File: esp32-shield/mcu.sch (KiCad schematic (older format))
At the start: 31 parts, among them J11 DNP, J5 Conn_01x14_Female, J6 Conn_01x14_Female, Q3 S8050, Q4 S8050, SW1 SKRKAEE020, U13 ESP32-WROOM32, U14 W25Q32JVSS, U4 SN74LV1T34DBV, U5 CH340C, U6 AMS1117-3.3, Y1 12MHZ

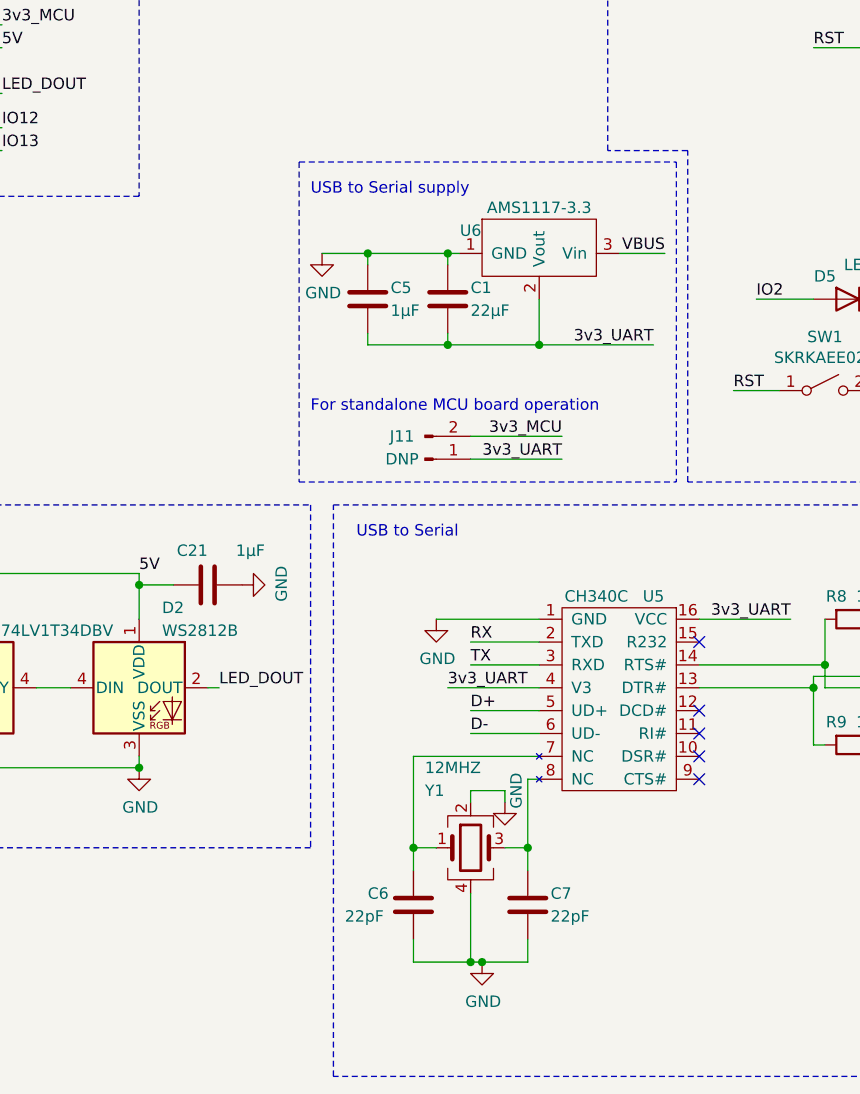
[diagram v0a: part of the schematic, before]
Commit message: changed CH340G to CH340C, deleted crystal footprint and caps, added caps
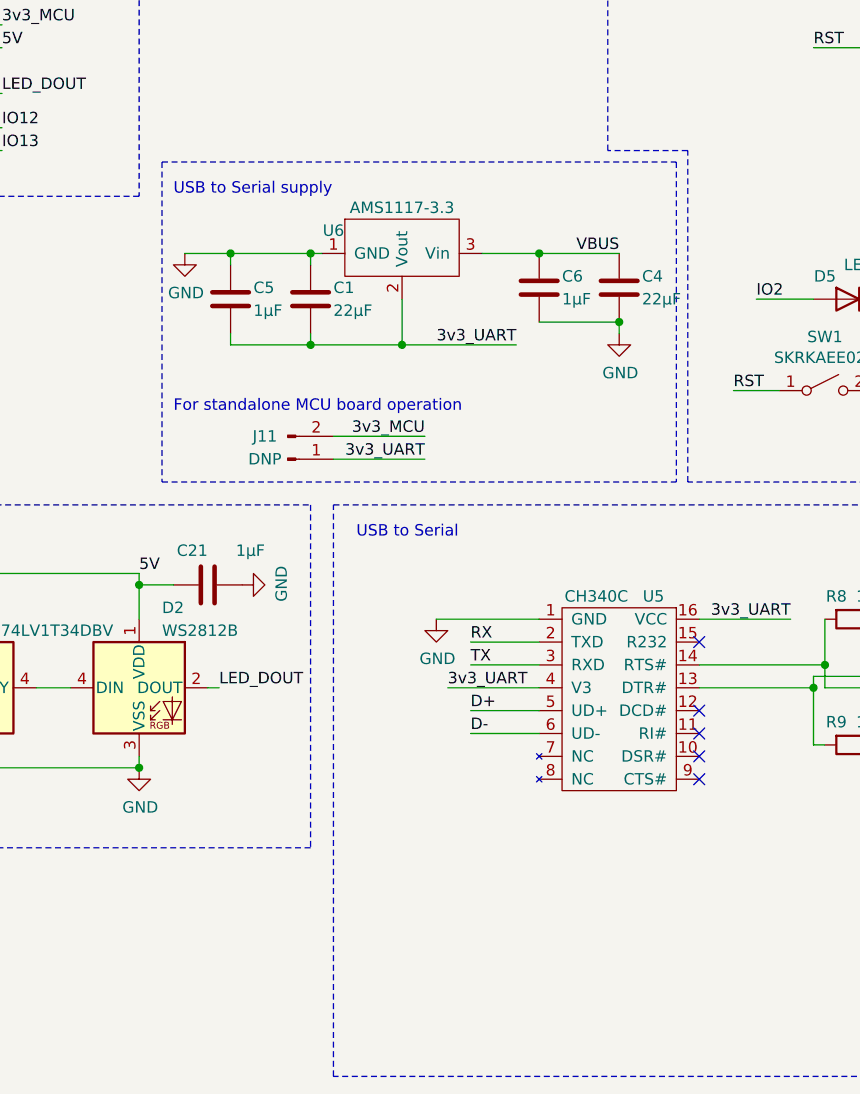
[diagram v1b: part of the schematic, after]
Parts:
- removed C7: 22pF, Capacitor_SMD:C_0603_1608Metric_Pad1.05x0.95mm_HandSolder, symbol Device:C
- removed Y1: 12MHZ, Crystal:Crystal_SMD_3225-4Pin_3.2x2.5mm_HandSoldering, symbol Device:Crystal_GND24
- added C4: 22µF, Capacitor_SMD:C_0805_2012Metric, symbol Device:C
- C19, C20, C21, C26, C5: footprint Capacitor_SMD:C_0603_1608Metric_Pad1.05x0.95mm_HandSolder -> Capacitor_SMD:C_0603_1608Metric
- C6: value 22pF -> 1µF; footprint Capacitor_SMD:C_0603_1608Metric_Pad1.05x0.95mm_HandSolder -> Capacitor_SMD:C_0603_1608Metric; DNP DNP -> (none); LCSC C1653 -> C15849
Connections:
- net GND: now also C4.2
- net VBUS: now also C6.1, C4.1
- net at U5.7 (NC): no longer C6.1
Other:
- moved on the sheet: C1, C5, J11, U6

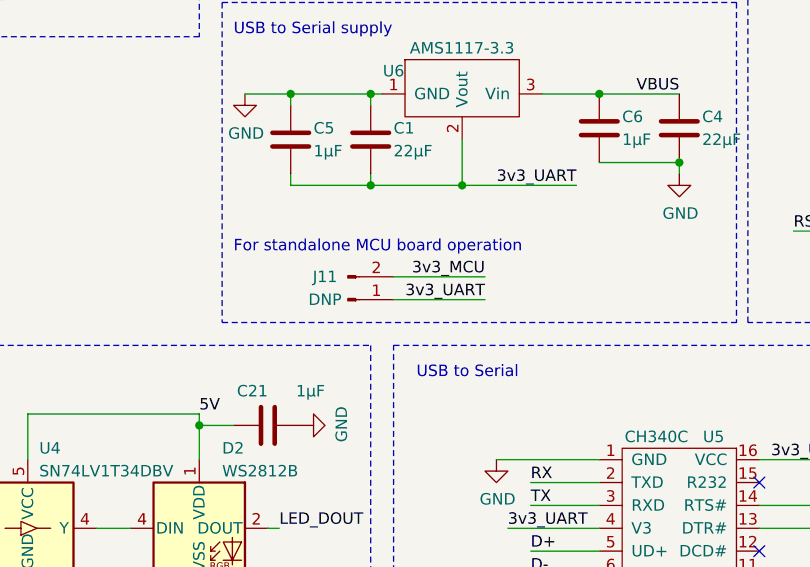
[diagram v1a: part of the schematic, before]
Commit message: swapped jumper with solderbridge
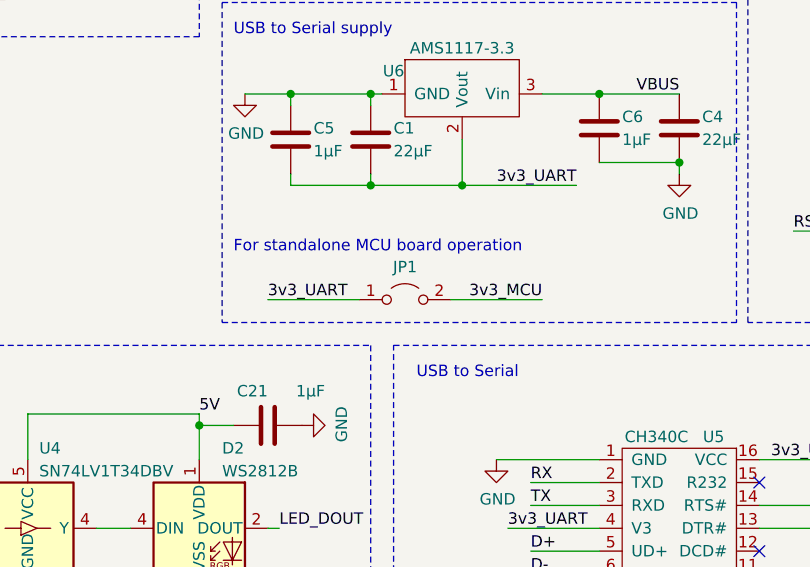
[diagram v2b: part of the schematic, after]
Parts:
- removed J11: DNP, Connector_PinHeader_2.54mm:PinHeader_1x02_P2.54mm_Vertical, symbol Connector:Conn_01x02_Male
- added JP1: Jumper_2_Open, Jumper:SolderJumper-2_P1.3mm_Open_Pad1.0x1.5mm, symbol Jumper:Jumper_2_Open
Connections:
- net 3v3_MCU: now also JP1.2 (B)
- net 3v3_UART: now also JP1.1 (A)
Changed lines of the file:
@@
 Wire Wire Line
 	5050 3450 5150 3450
-$Comp
-L Connector:Conn_01x02_Male J?
-U 1 1 6014FDBA
-P 2500 3750
-AR Path="/5F639CFE/6014FDBA" Ref="J?"  Part="1"
-AR Path="/5F639F48/6014FDBA" Ref="J?"  Part="1"
-AR Path="/5F63A193/6014FDBA" Ref="J11"  Part="1"
-F 0 "J11" H 2400 3650 50  0000 C CNN
-F 1 "DNP" H 2400 3750 50  0000 C CNN
-F 2 "Connector_PinHeader_2.54mm:PinHeader_1x02_P2.54mm_Vertical" H 2500 3750 50  0001 C CNN
-F 3 "" H 2500 3750 50  0001 C CNN
-F 4 "" H 2500 3750 50  0001 C CNN "LCSC"
-	1    2500 3750
-	1    0    0    1
-$EndComp
-Text Label 3100 3650 2    50   ~ 0
+Text Label 3350 3750 2    50   ~ 0
 3v3_MCU
 Wire Wire Line
-	3100 3650 2700 3650
-Text Label 3100 3750 2    50   ~ 0
+	3350 3750 2950 3750
+Text Label 2150 3750 0    50   ~ 0
 3v3_UART
 Wire Wire Line
-	2700 3750 3100 3750
+	2550 3750 2150 3750
 Wire Notes Line
 	1950 2450 1950 3850
@@
 	3950 3200 3950 3150
 Connection ~ 3950 3150
+$Comp
+L Jumper:Jumper_2_Open JP1
+U 1 1 60E8D0A3
+P 2750 3750
+F 0 "JP1" H 2750 3893 50  0000 C CNN
+F 1 "Jumper_2_Open" H 2750 3894 50  0001 C CNN
+F 2 "Jumper:SolderJumper-2_P1.3mm_Open_Pad1.0x1.5mm" H 2750 3750 50  0001 C CNN
+F 3 "~" H 2750 3750 50  0001 C CNN
+	1    2750 3750
+	1    0    0    -1
+$EndComp
 $EndSCHEMATC

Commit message: added part numbers and extended ref
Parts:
- D1: LCSC C8598 -> C8598
- D2: LCSC C114586 -> C2761795; extended part (none) -> extended
- J5, J6: LCSC (none) -> C124407; extended part (none) -> extended
- SW1, U4, U5: extended part (none) -> extended
- U13: LCSC C82899 -> C701342; extended part (none) -> extended
- U14: LCSC C25804 -> C82344; extended part (none) -> extended
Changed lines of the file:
@@
 F 2 "RF_Module:ESP32-WROOM-32" H 6900 2650 50  0001 C CNN
 F 3 "https://www.espressif.com/sites/default/files/documentation/esp32-wroom-32_datasheet_en.pdf" H 6850 1850 50  0001 C CNN
-F 4 "C82899" H 6850 1950 50  0001 C CNN "LCSC"
+F 4 "C701342" H 6850 1950 50  0001 C CNN "LCSC"
+F 5 "extended" H 6850 1950 50  0001 C CNN "extended part"
 	1    6850 1950
 	1    0    0    -1
@@
 F 3 "https://www.mpja.com/download/35227cpdata.pdf" H 4150 4750 50  0001 C CNN
 F 4 "C84681" H 3950 4550 50  0001 C CNN "LCSC"
+F 5 "extended" H 3950 4550 50  0001 C CNN "extended part"
 	1    3950 4550
 	1    0    0    -1
@@
 F 2 "Diode_SMD:D_SOD-123" H 5750 5250 50  0001 C CNN
 F 3 "https://datasheet.lcsc.com/szlcsc/Changjiang-Electronics-Tech-CJ-B5819W_C8598.pdf" H 5750 5250 50  0001 C CNN
-F 4 " C8598" H 5750 5250 50  0001 C CNN "LCSC"
+F 4 "C8598" H 5750 5250 50  0001 C CNN "LCSC"
 	1    5750 5250
 	1    0    0    -1
@@
 F 2 "Connector_PinSocket_2.54mm:PinSocket_1x14_P2.54mm_Vertical" H 10100 4100 50  0001 C CNN
 F 3 "~" H 10100 4100 50  0001 C CNN
+F 4 "C124407" H 10100 4100 50  0001 C CNN "LCSC"
+F 5 "extended" H 10100 4100 50  0001 C CNN "extended part"
 	1    10100 4100
 	1    0    0    -1
@@
 F 2 "Connector_PinSocket_2.54mm:PinSocket_1x14_P2.54mm_Vertical" H 10100 1650 50  0001 C CNN
 F 3 "~" H 10100 1650 50  0001 C CNN
+F 4 "C124407" H 10100 1650 50  0001 C CNN "LCSC"
+F 5 "extended" H 10100 1650 50  0001 C CNN "extended part"
 	1    10100 1650
 	1    0    0    -1
@@
 F 3 "~" H 4850 3450 50  0001 C CNN
 F 4 "C115357" H 4850 3450 50  0001 C CNN "LCSC"
+F 5 "extended" H 4850 3450 50  0001 C CNN "extended part"
 	1    4850 3450
 	1    0    0    -1
@@
 F 3 "http://www.winbond.com/resource-files/w25q32jv%20revg%2003272018%20plus.pdf" H 7850 5050 50  0001 C CNN
 F 4 "DNP" H 7850 5050 50  0001 C CNN "DNP"
-F 5 "C25804" H 7850 5050 50  0001 C CNN "LCSC"
+F 5 "C82344" H 7850 5050 50  0001 C CNN "LCSC"
+F 6 "extended" H 7850 5050 50  0001 C CNN "extended part"
 	1    7850 5050
 	1    0    0    -1
@@
 F 3 "https://www.ti.com/lit/ds/symlink/sn74lv1t34.pdf" H 700 4550 50  0001 C CNN
 F 4 "C100024" H 1100 4750 50  0001 C CNN "LCSC"
+F 5 "extended" H 1100 4750 50  0001 C CNN "extended part"
 	1    1100 4750
 	1    0    0    -1
@@
 F 2 "LED_SMD:LED_WS2812B_PLCC4_5.0x5.0mm_P3.2mm" H 1900 4450 50  0001 L TNN
 F 3 "https://cdn-shop.adafruit.com/datasheets/WS2812B.pdf" H 1950 4375 50  0001 L TNN
-F 4 "C114586" H 1850 4750 50  0001 C CNN "LCSC"
+F 4 "C2761795" H 1850 4750 50  0001 C CNN "LCSC"
+F 5 "extended" H 1850 4750 50  0001 C CNN "extended part"
 	1    1850 4750
 	1    0    0    -1
